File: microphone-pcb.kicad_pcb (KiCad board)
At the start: 4 copper layers, 10.7 x 11 mm, 9 parts, among them J1 Conn_FFC_Molex_5019510550

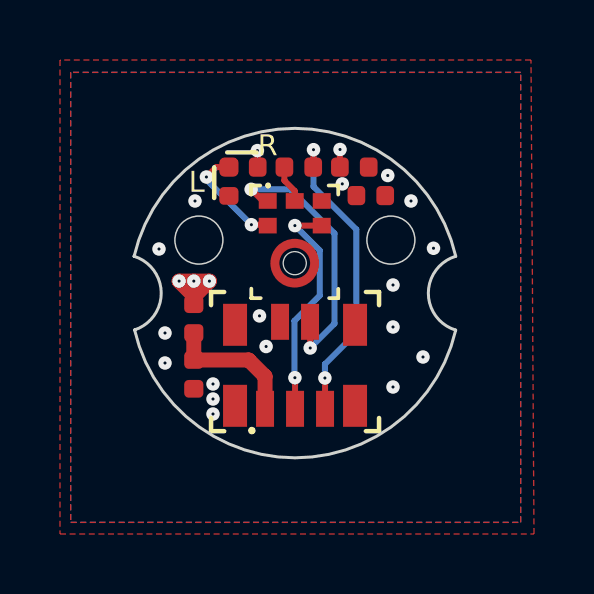
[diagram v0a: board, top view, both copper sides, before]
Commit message: [#71986] Import Changes to the PCB, Place TVS
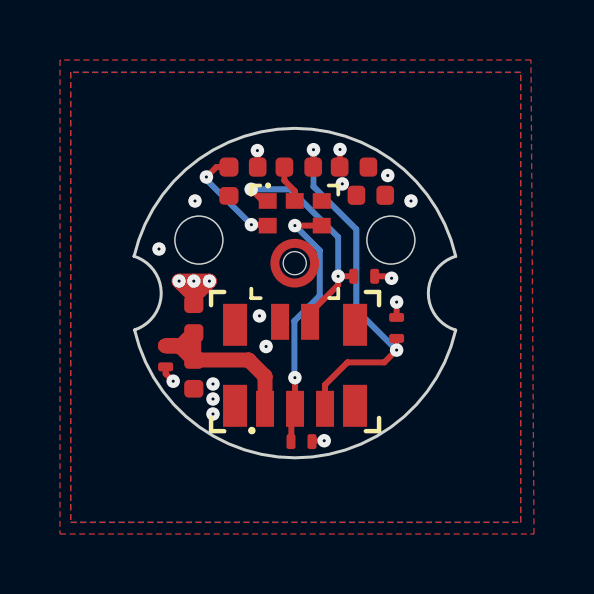
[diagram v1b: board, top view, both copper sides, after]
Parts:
- added D1: TPD1E0B04_XDFN-2, antmicro-footprints:XDFN-2_1x0.60mm, F.Cu at (235.7, 149.0)
- added D2: TPD1E0B04_XDFN-2, antmicro-footprints:XDFN-2_1x0.60mm, F.Cu at (240.2, 151.9)
- added D3: TPD1E0B04_XDFN-2, antmicro-footprints:XDFN-2_1x0.60mm, F.Cu at (242.3, 146.4)
- added D4: TPD1E0B04_XDFN-2, antmicro-footprints:XDFN-2_1x0.60mm, F.Cu at (243.4, 148.1)
- C1: value C_220p_0402 -> C_180p_0402
- C2: value C_100n_0402 -> C_100n_50V_X8L_0402
- moved C2 1.10 mm to (241.9, 142.7), turned to 180 degrees
- moved C1 1.09 mm to (242.5, 143.7)
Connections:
- C2 pad 1: VDD -> GND
- C2 pad 2: GND -> VDD
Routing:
- net VCC: track 4.58 -> 6.83 mm
- net /DATA: track 10.2 -> 12.5 mm
- net GND: track 0.00 -> 2.10 mm, vias 16 -> 13
- net /BCLK: track 7.75 -> 8.91 mm
- net /WS: track 9.13 -> 8.01 mm
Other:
- board text removed: "L"
- board text removed: "R"
